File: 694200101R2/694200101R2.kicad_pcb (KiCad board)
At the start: 2 copper layers, 438.6 x 125.8 mm, 401 parts, among them J1 USB_C_Receptacle_USB2.0, J2 Conn_01x06_Male, SW1 MX_SW, SW10 MX_SW, SW100 MX_SW, SW101 MX_SW, SW102 MX_SW, SW103 MX_SW, SW104 MX_SW, SW105 MX_SW, SW106 MX_SW, SW107 MX_SW, SW108 SW_SPST, SW109 SW_SPDT, SW11 MX_SW, SW12 MX_SW, SW13 MX_SW, SW14 MX_SW, SW15 MX_SW, SW16 MX_SW, SW17 MX_SW, SW18 MX_SW, SW19 MX_SW, SW2 MX_SW, SW20 MX_SW, SW21 MX_SW, SW22 MX_SW, SW23 MX_SW, SW24 MX_SW, SW25 MX_SW, SW26 MX_SW, SW27 MX_SW, SW28 MX_SW, SW29 MX_SW, SW3 MX_SW, SW30 MX_SW, SW31 MX_SW, SW32 MX_SW, SW33 MX_SW, SW34 MX_SW, SW35 MX_SW, SW36 MX_SW, SW37 MX_SW, SW38 MX_SW, SW39 MX_SW, SW4 MX_SW, SW40 MX_SW, SW41 MX_SW, SW42 MX_SW, SW43 MX_SW, SW44 MX_SW, SW45 MX_SW, SW46 MX_SW, SW47 MX_SW, SW48 MX_SW, SW49 MX_SW, SW5 MX_SW, SW50 MX_SW, SW51 MX_SW, SW52 MX_SW, SW53 MX_SW, SW54 MX_SW, SW55 MX_SW, SW56 MX_SW, SW57 MX_SW, SW58 MX_SW, SW59 MX_SW, SW6 MX_SW, SW60 MX_SW, SW61 MX_SW, SW62 MX_SW, SW63 MX_SW, SW64 MX_SW, SW65 MX_SW, SW66 MX_SW, SW67 MX_SW, SW68 MX_SW, SW69 MX_SW, SW7 MX_SW, SW70 MX_SW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

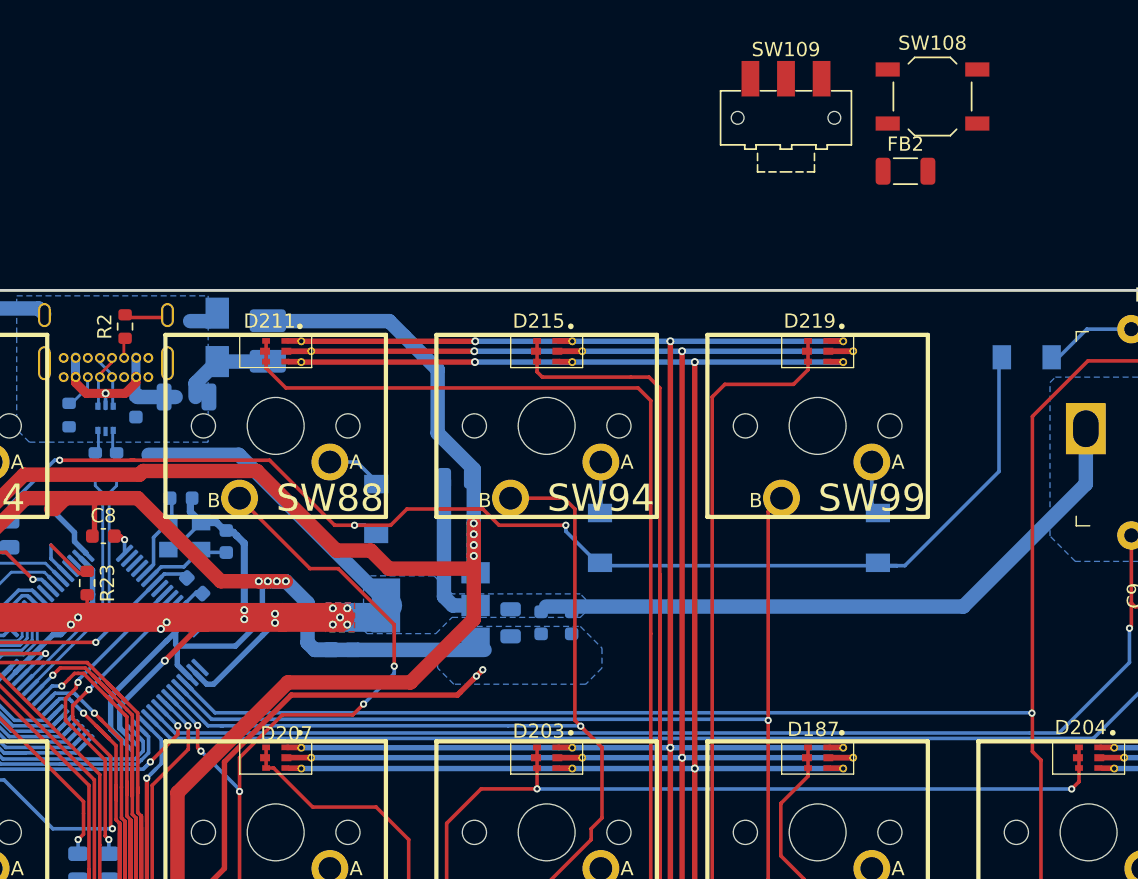
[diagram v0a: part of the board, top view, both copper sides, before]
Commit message: Hooked up Reset and Boot Set switch
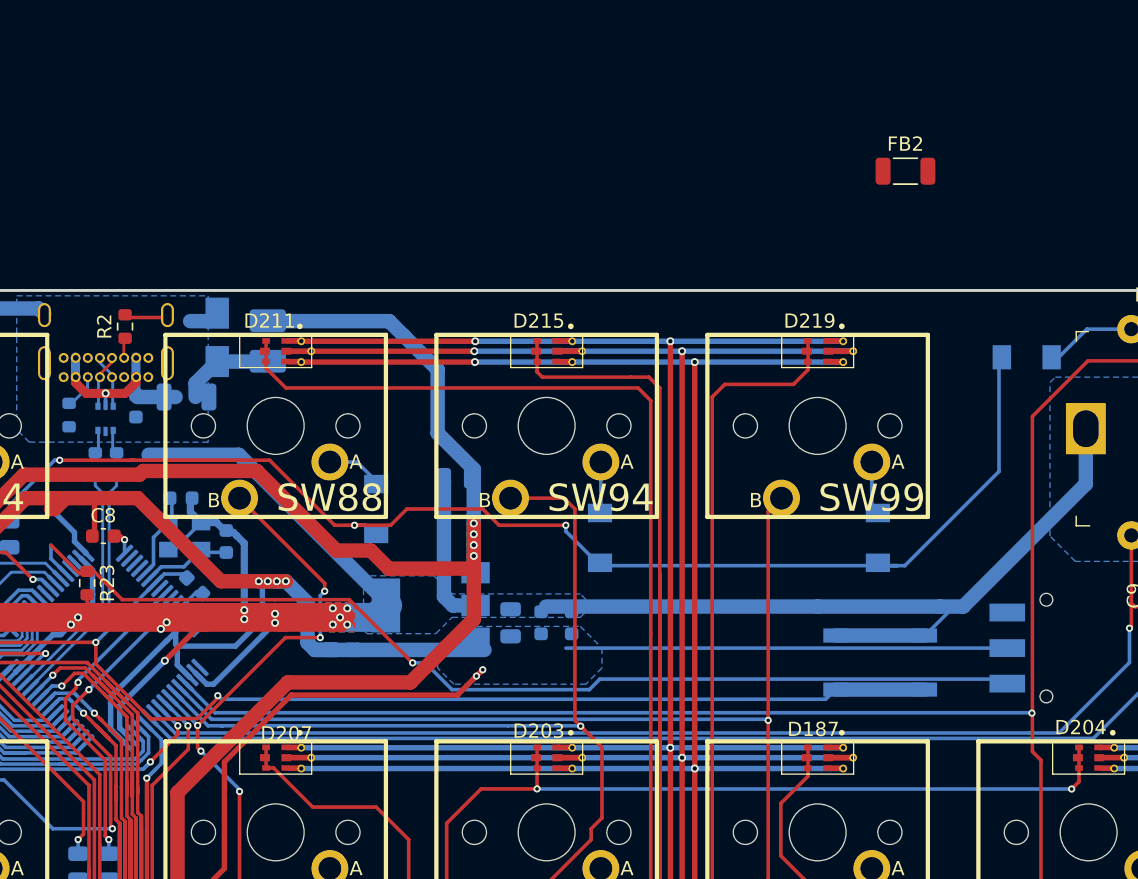
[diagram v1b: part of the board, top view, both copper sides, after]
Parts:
- SW108, SW109: moved to B.Cu
- moved SW109 41.5 mm to (421.1, 25.1), turned to 270 degrees
- moved SW108 40.0 mm to (409.4, 26.2)
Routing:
- net /BOOT0: track 5.78 -> 74.4 mm, vias 0 -> 1
- net /RST: track 52.3 -> 115.1 mm, vias 2 -> 3
- net +3V3: track 756.1 -> 787.1 mm
- net /COL_19: track 133.8 -> 123.9 mm
- net GND: track 619.4 -> 629.2 mm
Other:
- net class Power added: clearance 0.1016, trace_width 0.2032, via_dia 0.508, via_drill 0.254

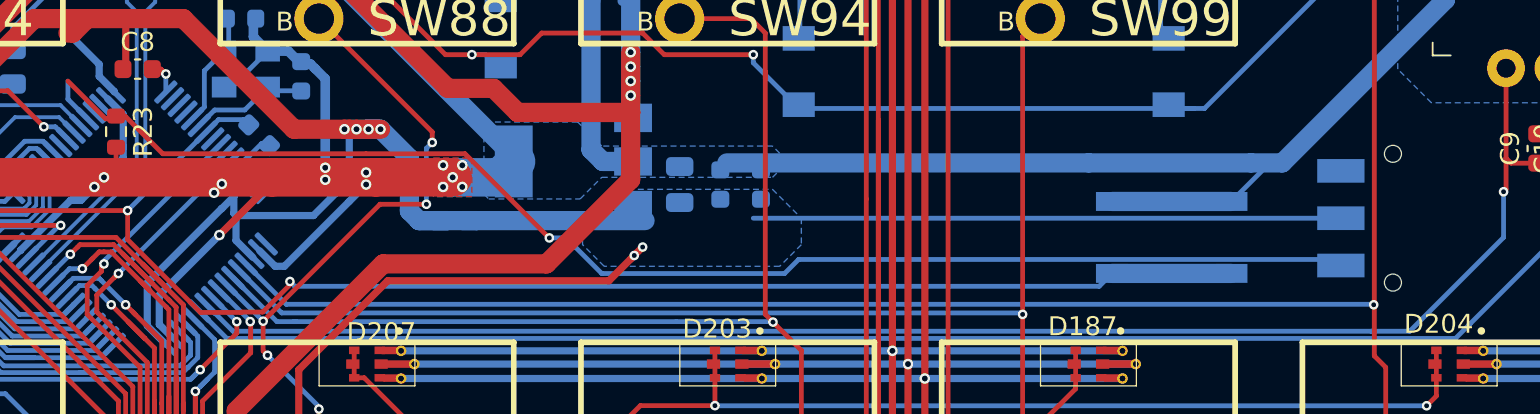
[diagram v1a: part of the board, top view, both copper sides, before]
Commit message: Change BOOT0 Switch to one that's lower profile
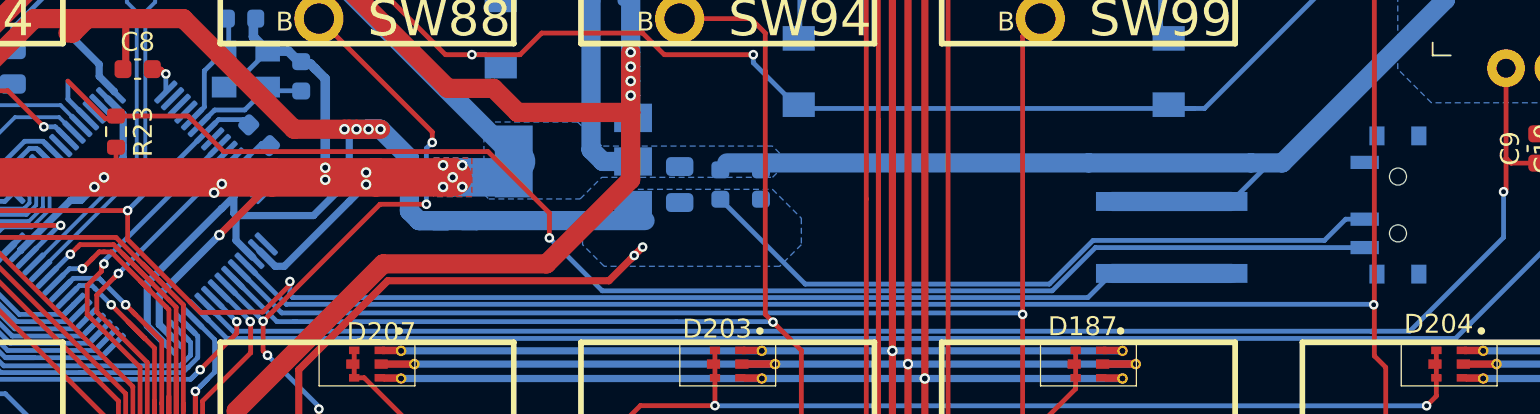
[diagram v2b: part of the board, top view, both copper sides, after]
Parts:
- SW109: footprint cldg:SW_SPDT_CK-JS102011SAQN -> Button_Switch_SMD:SW_SPDT_PCM12
- moved SW109 0.70 mm to (421.1, 24.4)
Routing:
- net +3V3: track 787.1 -> 793.4 mm
- net /BOOT0: track 74.4 -> 77.3 mm
- net /RST: track 115.1 -> 116.0 mm

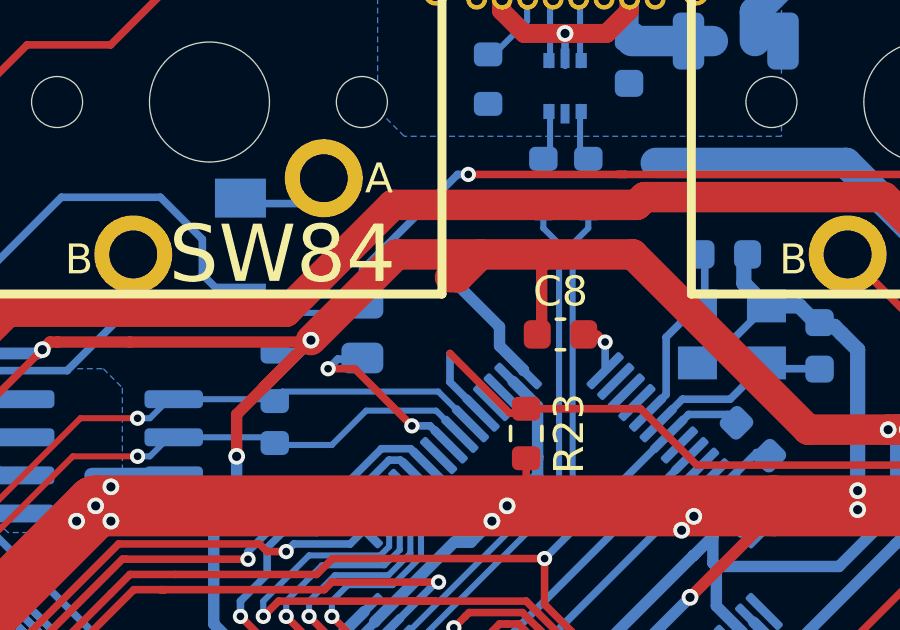
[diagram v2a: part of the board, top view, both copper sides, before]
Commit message: Update fuse 3D Model and attach some missing nets
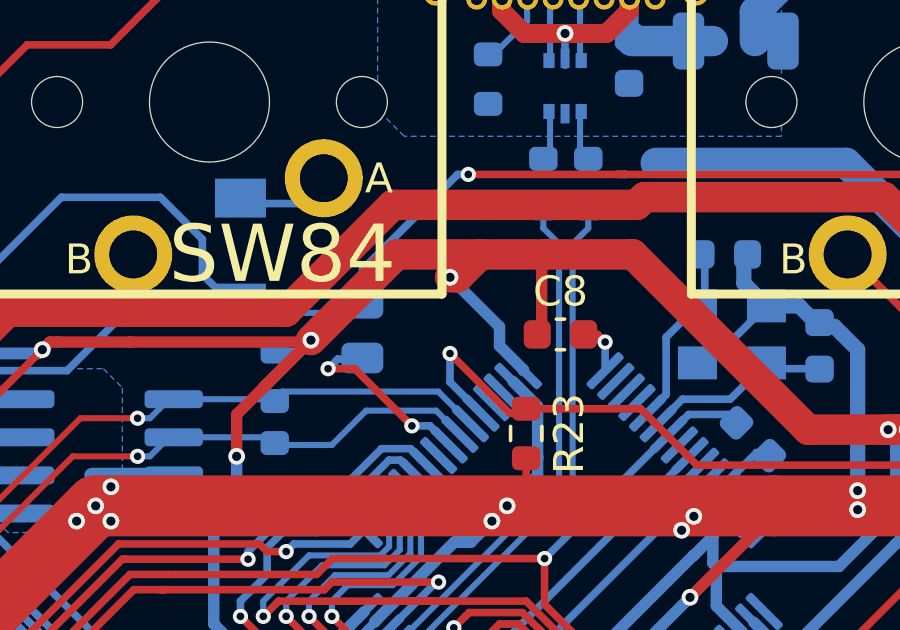
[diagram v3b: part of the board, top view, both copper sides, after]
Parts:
- F1: footprint Fuse:Fuse_1210_3225Metric_Castellated -> cldg:Fuse_1210_3225Metric_Castellated
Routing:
- net /BOOT0: vias 1 -> 2
- net +3V3: vias 14 -> 15

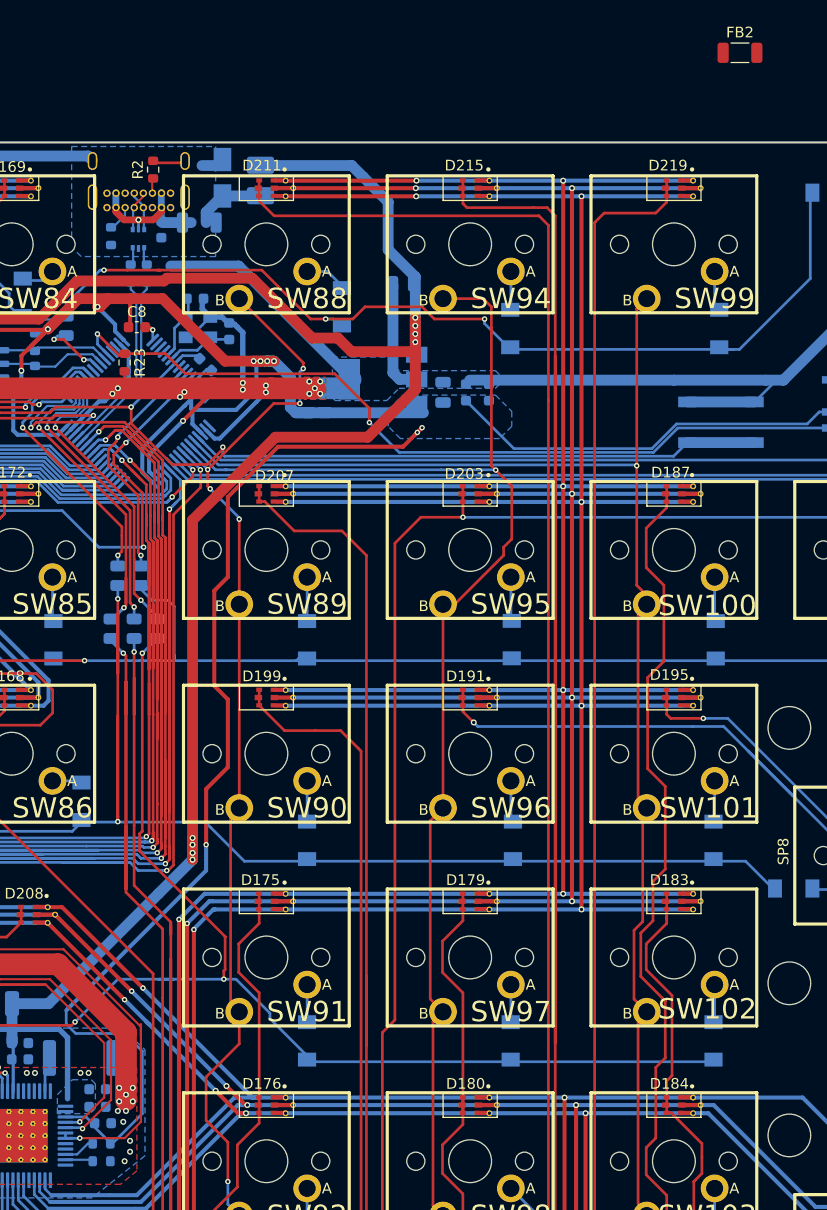
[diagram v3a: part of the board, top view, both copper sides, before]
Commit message: fied to latest power
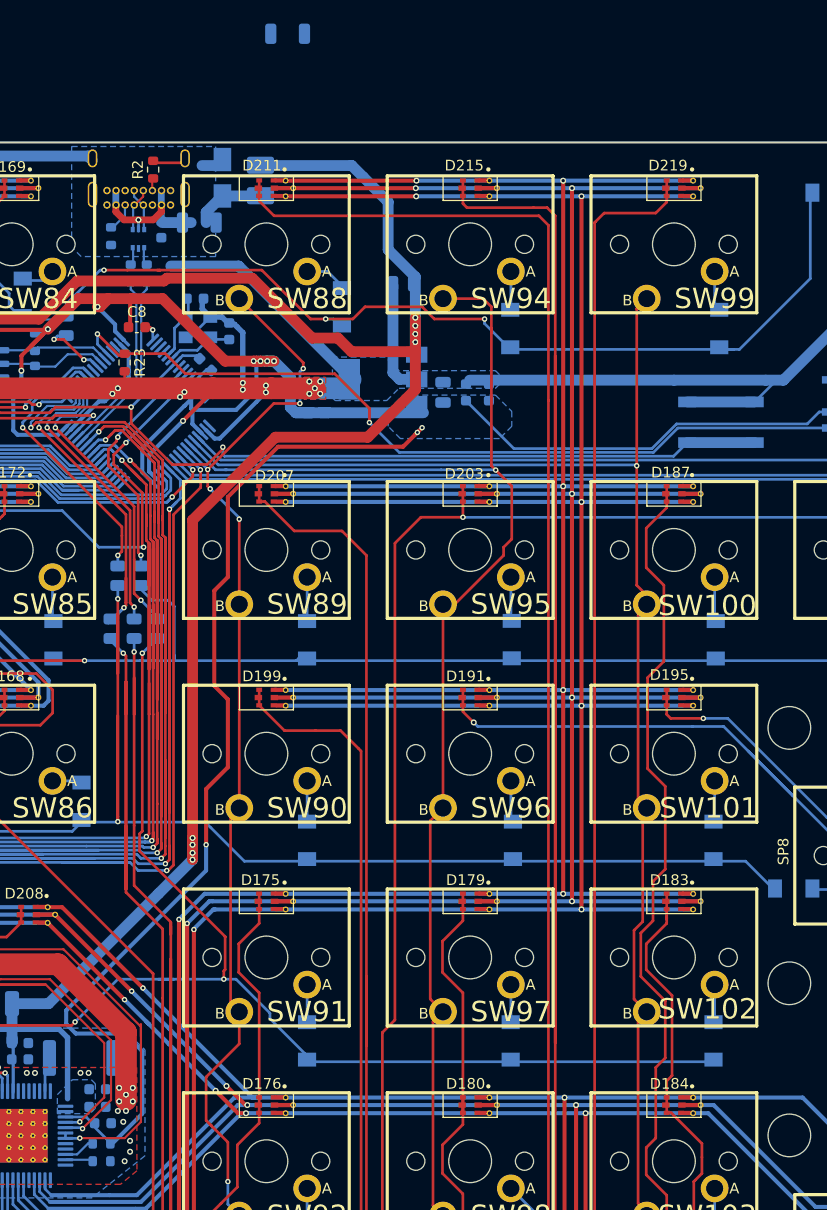
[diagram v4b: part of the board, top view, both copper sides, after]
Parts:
- FB2: moved to B.Cu
- moved FB2 42.3 mm to (368.9, -10.2)
- moved J1 0.25 mm to (352.0, 5.85)
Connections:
- CR1 pad 1: VCC -> Net-(CR1-Pad1)
- F1 pad 2: Net-(F1-Pad2) -> Net-(CR1-Pad1)
- FB1 pad 1: Net-(F1-Pad2) -> Net-(CR1-Pad1)

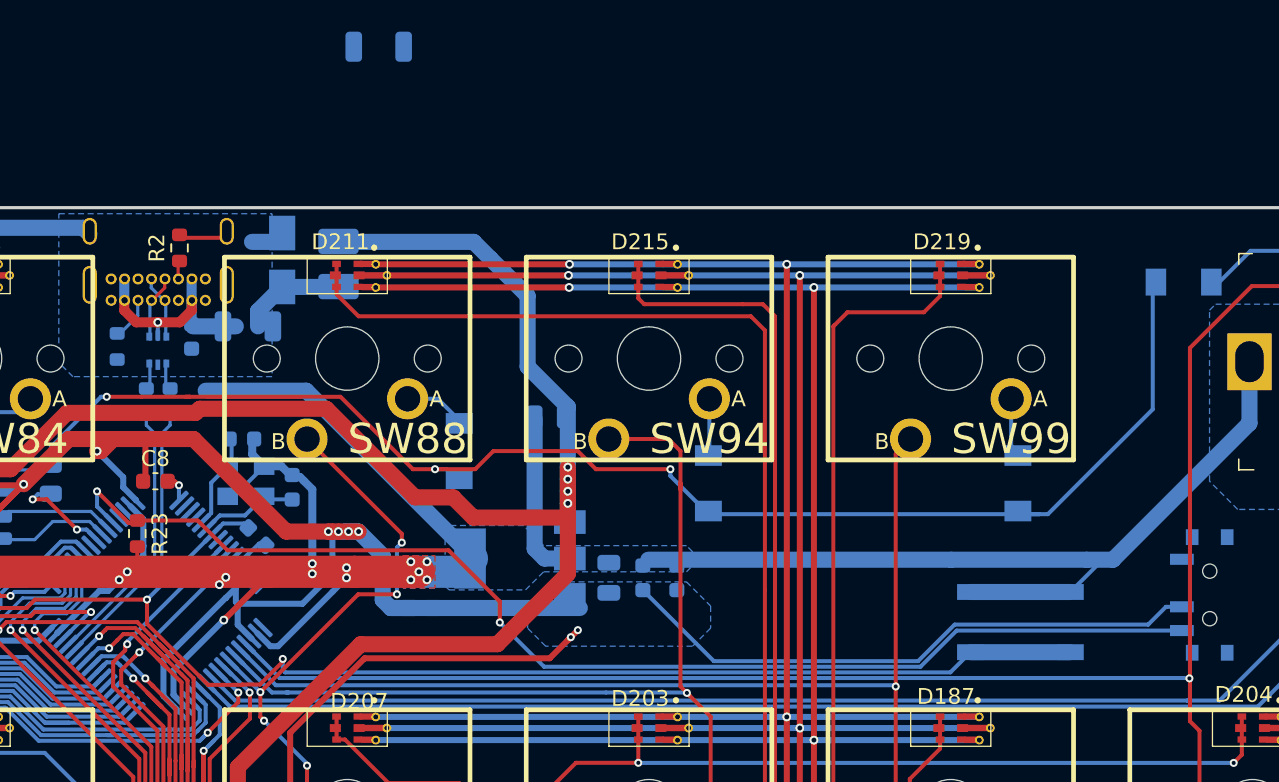
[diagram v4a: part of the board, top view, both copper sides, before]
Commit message: fix reset and programming switches
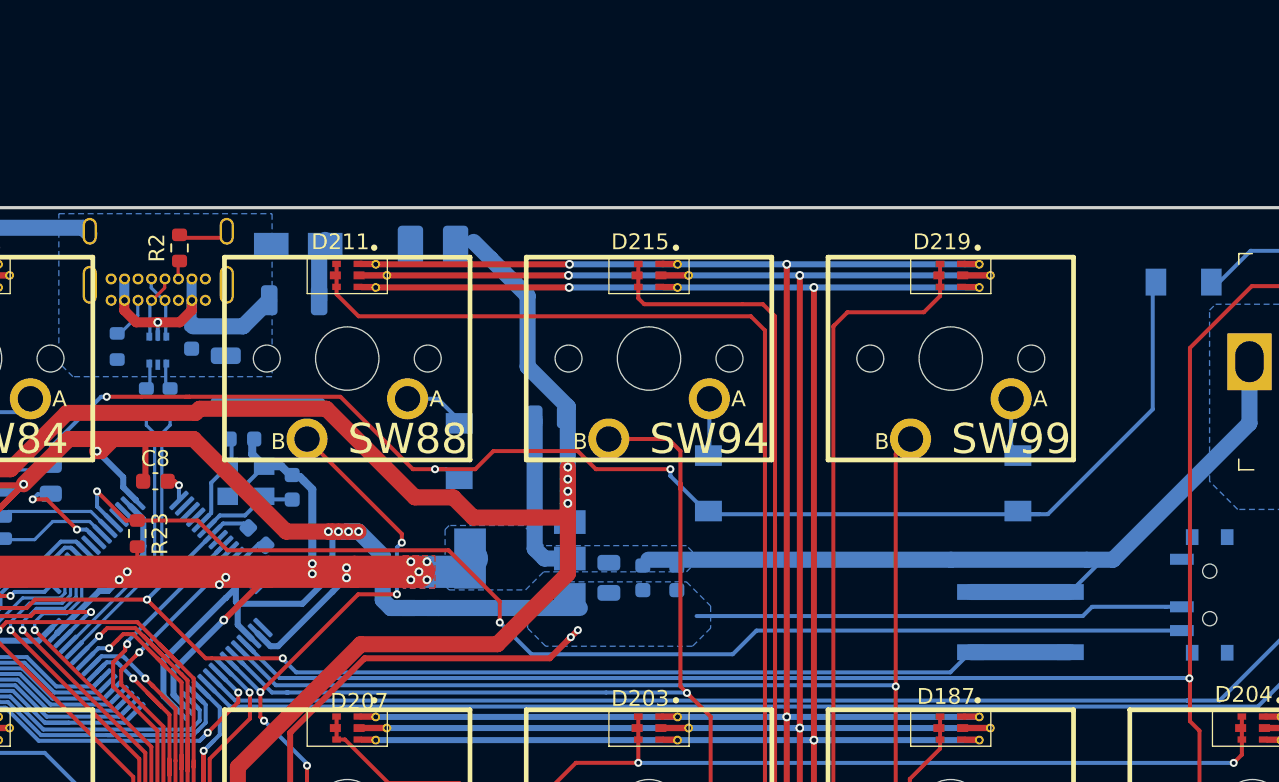
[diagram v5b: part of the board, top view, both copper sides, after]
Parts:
- moved FB2 23.2 mm to (359.3, 10.9), turned to 270 degrees
- moved F1 6.08 mm to (372.4, 2.41), turned to 180 degrees
- moved FB1 3.36 mm to (363.6, 5.84)
- moved CR1 1.35 mm to (363.9, 2.41), turned to 180 degrees
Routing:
- net VCC: track 526.0 -> 510.0 mm
- net GND: track 629.2 -> 614.4 mm
- net +3V3: track 793.4 -> 787.0 mm
- net Net-(CR1-Pad1): track 0.00 -> 3.97 mm
- net VBUS: track 13.7 -> 16.5 mm
- net /RST: track 116.0 -> 113.2 mm
- net Earth: track 64.0 -> 62.7 mm
- net /BOOT0: track 77.3 -> 76.6 mm

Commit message: LDO and gnd
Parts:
- moved C25 4.45 mm to (379.9, 17.7)
- moved FB2 2.22 mm to (361.2, 12.1), turned to 0 degrees
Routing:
- net GND: track 614.4 -> 604.0 mm
- net Net-(CR1-Pad1): track 3.97 -> 9.35 mm
- net /ROW_0: track 431.0 -> 434.1 mm
- net /COL_20: track 127.2 -> 124.6 mm
- net Earth: track 62.7 -> 65.0 mm
- net VCC: track 510.0 -> 511.8 mm, vias 12 -> 10

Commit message: only driver 1 left
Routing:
- net GND: vias 58 -> 56
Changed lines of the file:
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@@
     (thickness 1.6)
     (drawings 2092)
-    (tracks 5285)
+    (tracks 5283)
     (zones 0)
     (modules 401)
@@
   (segment (start 298.958 76.835) (end 294.005 71.882) (width 2.032) (layer F.Cu) (net 2))
   (segment (start 339.217 76.835) (end 298.958 76.835) (width 2.032) (layer F.Cu) (net 2))
-  (via (at 353.822 90.551) (size 0.5588) (drill 0.3048) (layers F.Cu B.Cu) (net 2))
-  (via (at 353.06 90.551) (size 0.5588) (drill 0.3048) (layers F.Cu B.Cu) (net 2))
-  (via (at 353.695 95.25) (size 0.5588) (drill 0.3048) (layers F.Cu B.Cu) (net 2))
+  (via (at 353.06 90.424) (size 0.5588) (drill 0.3048) (layers F.Cu B.Cu) (net 2))
+  (via (at 353.314 95.377) (size 0.5588) (drill 0.3048) (layers F.Cu B.Cu) (net 2))
   (via (at 353.822 89.027) (size 0.5588) (drill 0.3048) (layers F.Cu B.Cu) (net 2))
   (via (at 354.457 88.392) (size 0.5588) (drill 0.3048) (layers F.Cu B.Cu) (net 2))
@@
   (via (at 353.187 88.392) (size 0.5588) (drill 0.3048) (layers F.Cu B.Cu) (net 2) (status 30))
   (via (at 353.568 91.567) (size 0.5588) (drill 0.3048) (layers F.Cu B.Cu) (net 2))
-  (via (at 354.203 94.361) (size 0.5588) (drill 0.3048) (layers F.Cu B.Cu) (net 2))
-  (via (at 354.203 93.345) (size 0.5588) (drill 0.3048) (layers F.Cu B.Cu) (net 2))
+  (via (at 348.361 96.52) (size 0.5588) (drill 0.3048) (layers F.Cu B.Cu) (net 2))
   (segment (start 430.513006 20.811006) (end 430.53 20.828) (width 0.508) (layer F.Cu) (net 2) (status 30))
   (segment (start 429.6056 20.7926) (end 429.624006 20.811006) (width 0.508) (layer F.Cu) (net 2))
@@
   (via (at 31.75 27.94) (size 0.5588) (drill 0.3048) (layers F.Cu B.Cu) (net 2))
   (segment (start 42.799 13.462) (end 41.783 13.462) (width 2.032) (layer F.Cu) (net 2))
-  (segment (start 41.783 13.462) (end 39.878 11.557) (width 2.032) (layer F.Cu) (net 2))
-  (segment (start 39.878 11.557) (end 37.465 11.557) (width 2.032) (layer F.Cu) (net 2))
+  (segment (start 41.783 11.684) (end 39.878 9.779) (width 2.032) (layer F.Cu) (net 2))
+  (segment (start 39.751 9.906) (end 37.338 9.906) (width 2.032) (layer F.Cu) (net 2))
   (segment (start 30.734 18.923) (end 30.734 16.383) (width 0.254) (layer F.Cu) (net 2))
   (segment (start 351.29927 24.1935) (end 351.8535 24.1935) (width 0.381) (layer B.Cu) (net 2))
